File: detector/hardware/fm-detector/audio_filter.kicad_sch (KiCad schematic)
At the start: 11 parts, among them J3 U.FL, Q3 BSS138

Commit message: pulse detector design
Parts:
- removed C11: 4.7n, g-cap:C_0603_1608Metric, symbol #gplm:cap/CAP-0000-0472
- removed C12, C13, C14: 1.5n, g-cap:C_0603_1608Metric, symbol #gplm:cap/CAP-0000-0152
- removed C26: 100n, g-cap:C_0603_1608Metric, symbol #gplm:cap/CAP-0000-0104
- removed J3: U.FL, g-con:U.FL_Hirose_U.FL-R-SMT-1_Vertical, symbol #gplm:con/CON-0001-0000
- removed L4: 3µ9, g-ind:L_Coilcraft_1008HQ_2520Metric, symbol #gplm:ind/IND-0002-0392
- removed L5: 8µ2, g-ind:L_Coilcraft_1008HQ_2520Metric, symbol #gplm:ind/IND-0002-0822
- removed L6: 2µ7, g-ind:L_Coilcraft_1008HQ_2520Metric, symbol #gplm:ind/IND-0002-0272
- removed Q3: BSS138, g-SOT:SOT-23-3, symbol #gplm:trs/TRS-0001-0000
- removed RV1: 10K, g-rvr:Potentiometer_Bourns_3314J_Vertical, symbol #gplm:rvr/RVR-0000-1002
- added C27, C30: 100n, g-cap:C_0603_1608Metric, symbol #gplm:cap/CAP-0000-0104
- added C28: 1.5n, g-cap:C_0603_1608Metric, symbol #gplm:cap/CAP-0000-0152
- added C29: 820p, g-cap:C_0603_1608Metric, symbol #gplm:cap/CAP-0000-0821
- added Q9: MMBT3904, g-SOT:SOT-23-3, symbol #gplm:trs/TRS-0000-0001
- added R10: 150K, g-res:R_0603_1608Metric, symbol #gplm:res/RES-0000-1503
- added R25: 39K, g-res:R_0603_1608Metric, symbol #gplm:res/RES-0000-3902
- added R26: 3K3, g-res:R_0603_1608Metric, symbol #gplm:res/RES-0000-3301
- added R27: 15K, g-res:R_0603_1608Metric, symbol #gplm:res/RES-0000-1502
- added R28: 10K, g-res:R_0603_1608Metric, symbol #gplm:res/RES-0000-1002
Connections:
- net +5V: now also C30.2, Q9.3 (C), R25.2
- net GND: now also C29.1, C30.1, R10.1, R28.1
- new net: C28.2, R26.1, R27.2
- new net: C29.2, Q9.1 (B), R10.2, R25.1, R26.2
- new net: C27.2, R27.1
- new net IN: C27.1
- new net OUT: C28.1, Q9.2 (E), R28.2
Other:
- title: IF2 Mixer -> Audio filter

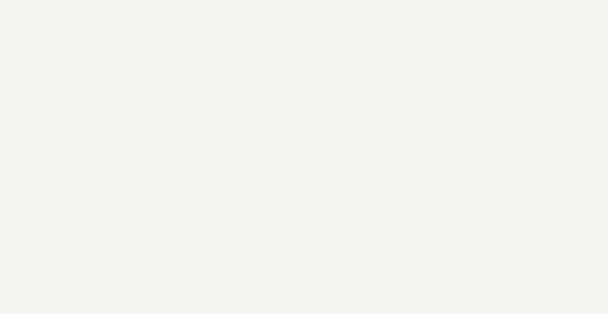
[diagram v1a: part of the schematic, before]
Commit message: Schematic for PCB-0010-0100
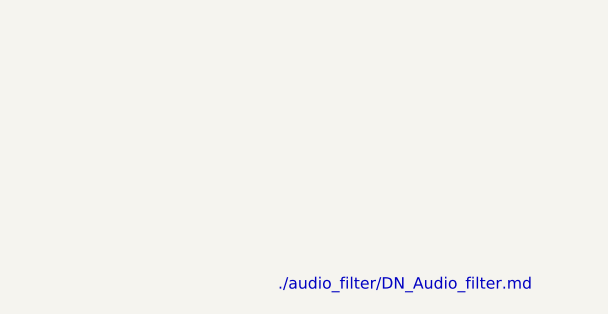
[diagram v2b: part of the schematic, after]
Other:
- note added: "./audio_filter/DN_Audio_filter.md"
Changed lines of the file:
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@@
 		(title "Audio filter")
+	)
+	(text "./audio_filter/DN_Audio_filter.md"
+		(exclude_from_sim no)
+		(at 118.11 129.54 0)
+		(effects
+			(font
+				(size 1.27 1.27)
+			)
+			(href "https://github.com/LieBtrau/MegawattKS_Radio_Design_101/blob/main/audio_filter/DN_Audio_filter.md")
+		)
 	)
 	(junction
